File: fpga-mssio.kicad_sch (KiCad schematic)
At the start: 15 parts, among them U1 MPFS250T-FCVG484, U30 NTS0102_XSON

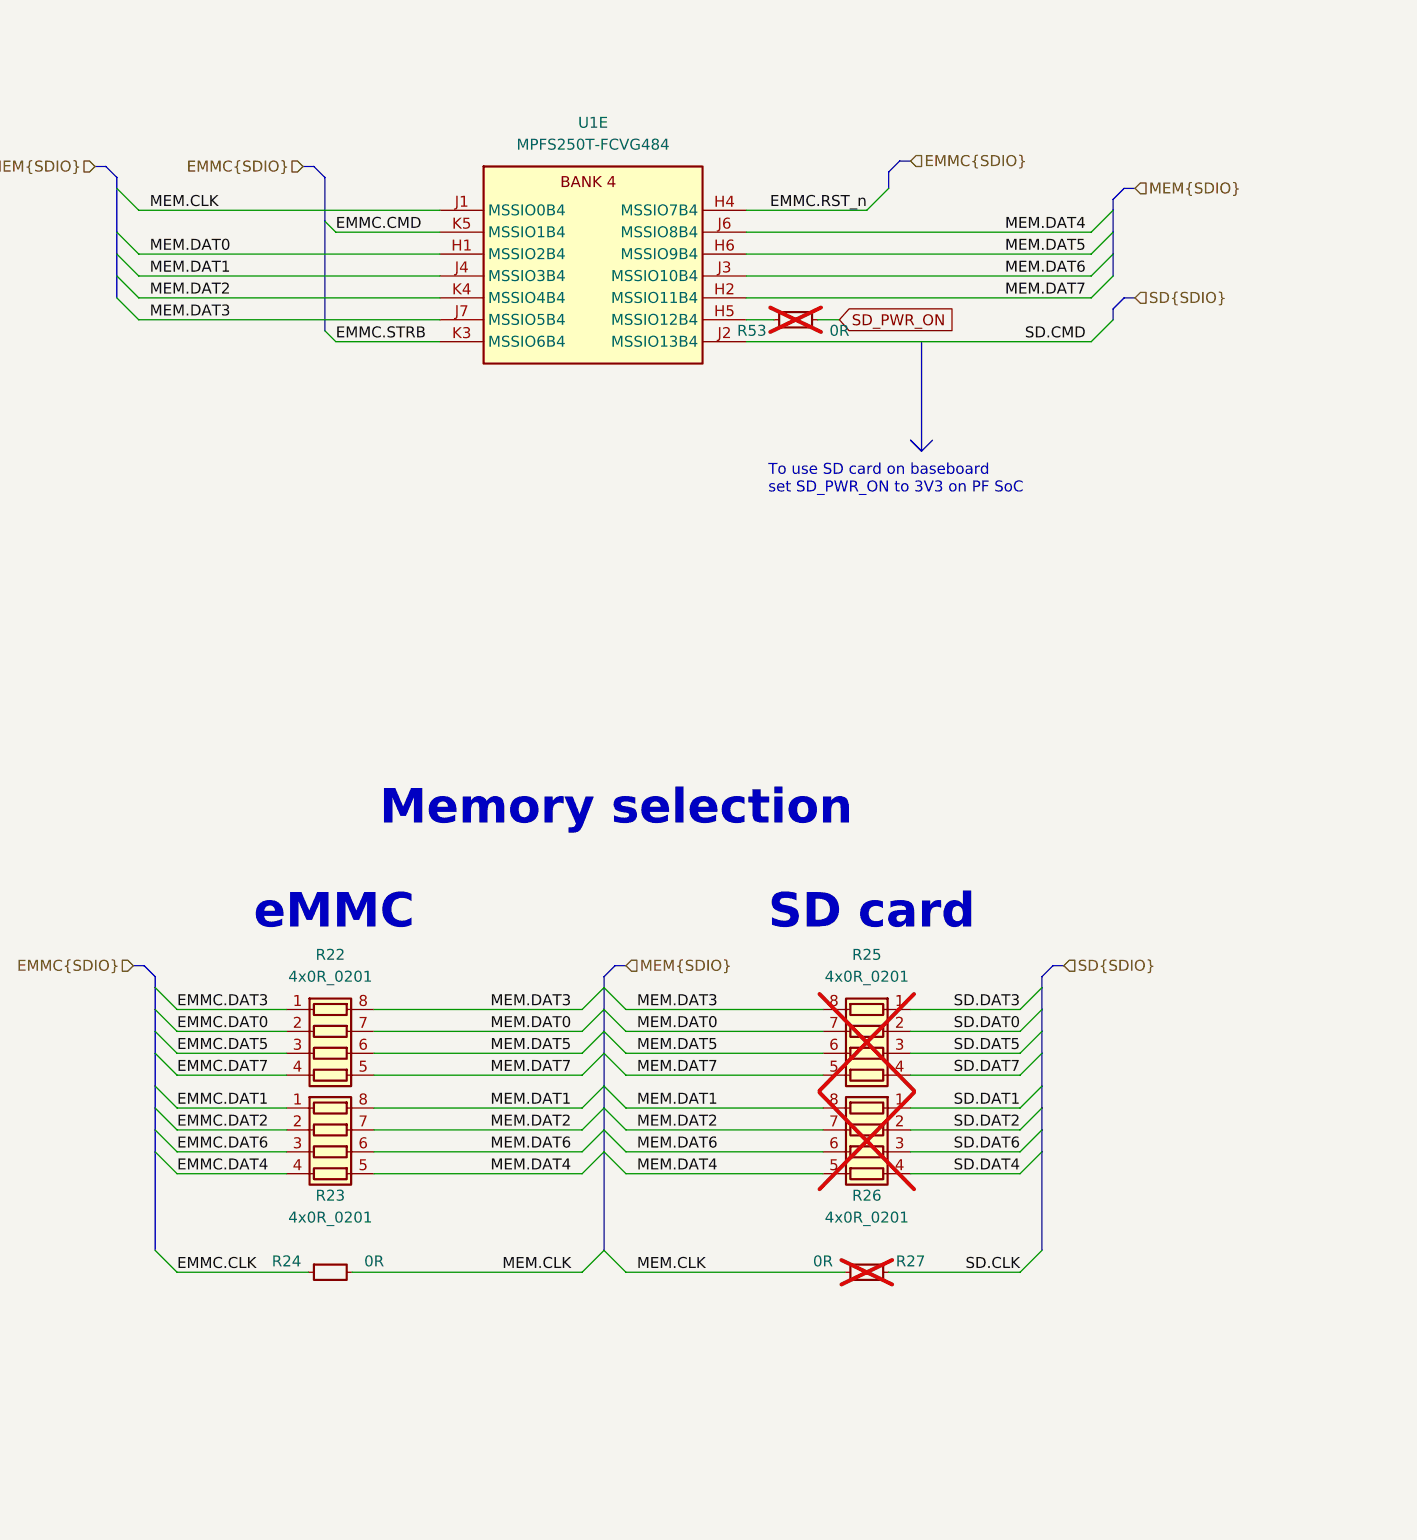
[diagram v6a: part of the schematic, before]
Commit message: [#57970] Update SD connection
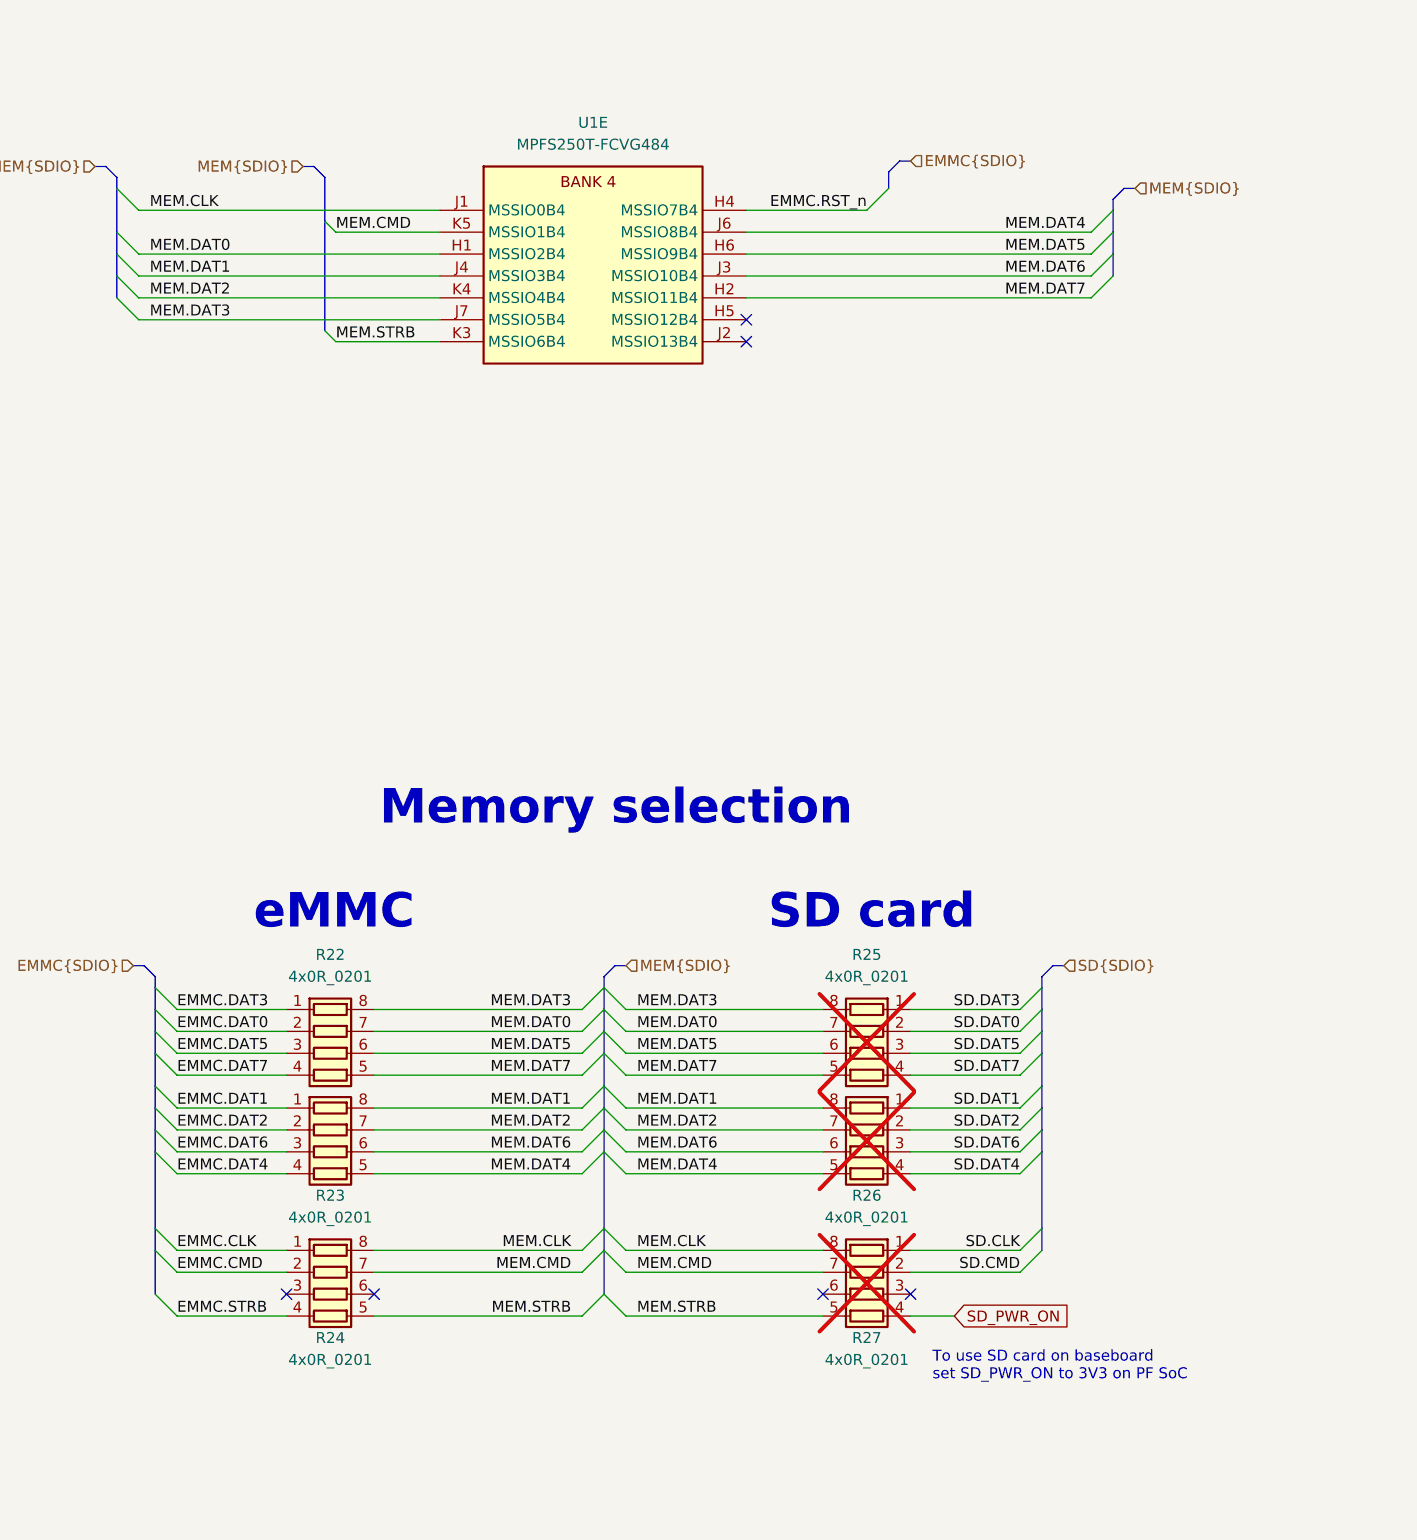
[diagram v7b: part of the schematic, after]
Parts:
- removed R24, R27, R53: R_0R_0402, antmicro-footprints:R_0402_1005Metric, symbol antmicroResistors0402:R_0R_0402
- added R24, R27: R_4x0R_0201_array, antmicro-footprints:R_Array_4x0201_Panasonic_EXB18V, symbol antmicroResistorNetworksArrays:R_4x0R_0201_array
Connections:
- net EMMC.CLK: now also R24.1 (R1.1)
- net EMMC.CMD: now also R24.2 (R2.1); no longer U1.K5 (MSSIO1B4)
- net EMMC.STRB: now also R24.4 (R4.1); no longer U1.K3 (MSSIO6B4)
- net MEM.CLK: now also R24.8 (R1.2), R27.8 (R1.2)
- net SD.CLK: now also R27.1 (R1.1)
- net SD.CMD: now also R27.2 (R2.1); no longer U1.J2 (MSSIO13B4)
- net SD_PWR_ON: now also R27.4 (R4.1)
- new net MEM.CMD: R24.7 (R2.2), R27.7 (R2.2), U1.K5 (MSSIO1B4)
- new net MEM.STRB: R24.5 (R4.2), R27.5 (R4.2), U1.K3 (MSSIO6B4)
- no-connect marks 6 -> 12

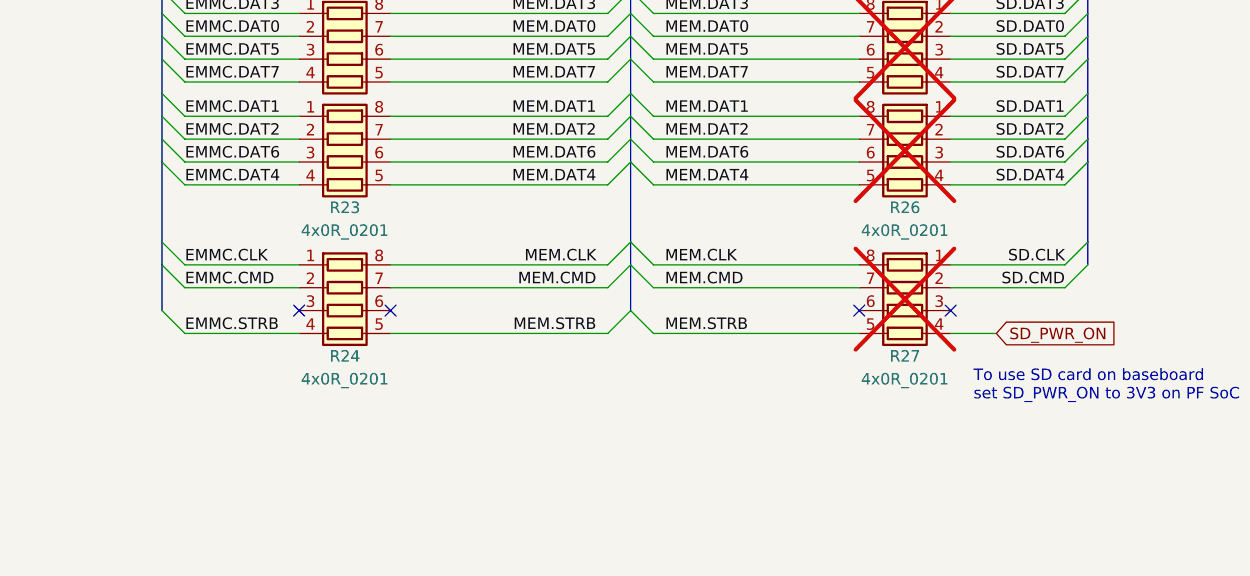
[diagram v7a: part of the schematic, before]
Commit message: [#57970] Improve SD card connection
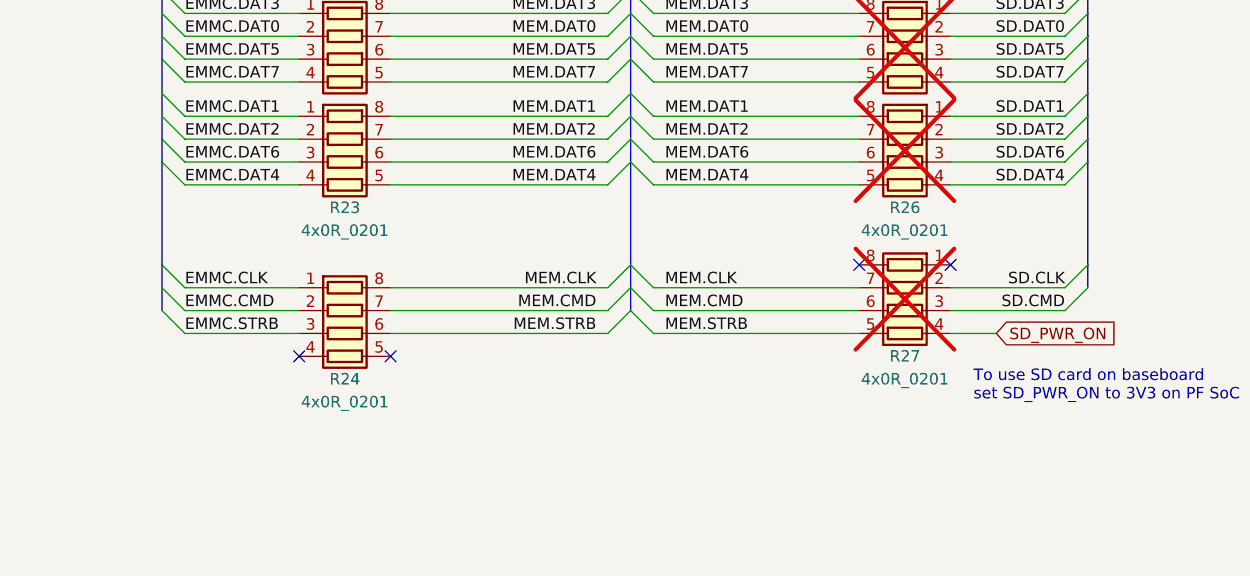
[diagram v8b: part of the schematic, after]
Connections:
- net EMMC.STRB: now also R24.3 (R3.1); no longer R24.4 (R4.1)
- net MEM.CLK: now also R27.7 (R2.2); no longer R27.8 (R1.2)
- net MEM.CMD: now also R27.6 (R3.2); no longer R27.7 (R2.2)
- net MEM.STRB: now also R24.6 (R3.2); no longer R24.5 (R4.2)
- net SD.CLK: now also R27.2 (R2.1); no longer R27.1 (R1.1)
- net SD.CMD: now also R27.3 (R3.1); no longer R27.2 (R2.1)
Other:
- moved on the sheet: R24
